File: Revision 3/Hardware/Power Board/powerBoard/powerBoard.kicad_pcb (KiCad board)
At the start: 2 copper layers, 92 x 91.5 mm, 31 parts, among them J1 1366005, J2 1366005, J3 Conn_01x03, J7 Conn_01x02, SW1 SW_SPST, U2 MOC3083S-TA1

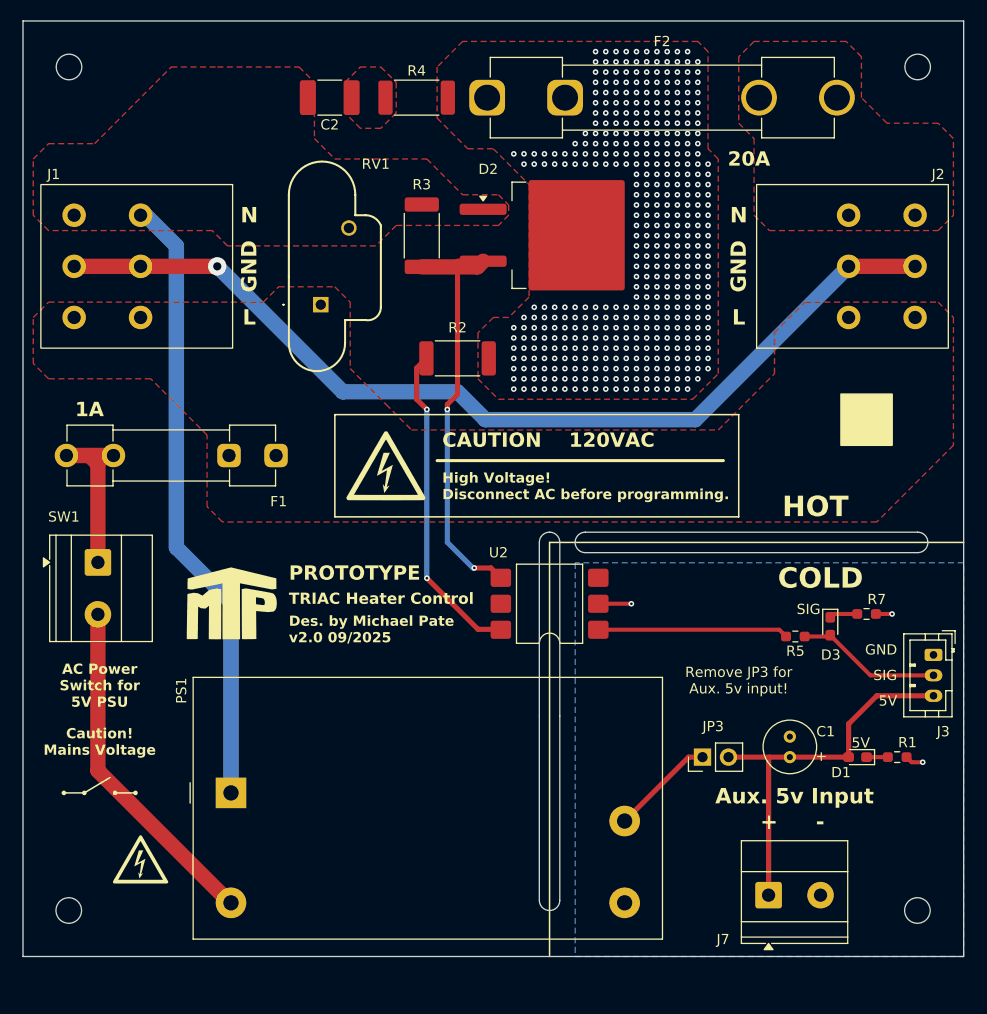
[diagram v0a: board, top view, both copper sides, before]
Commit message: Fix 3D Models, readjust traces on power board
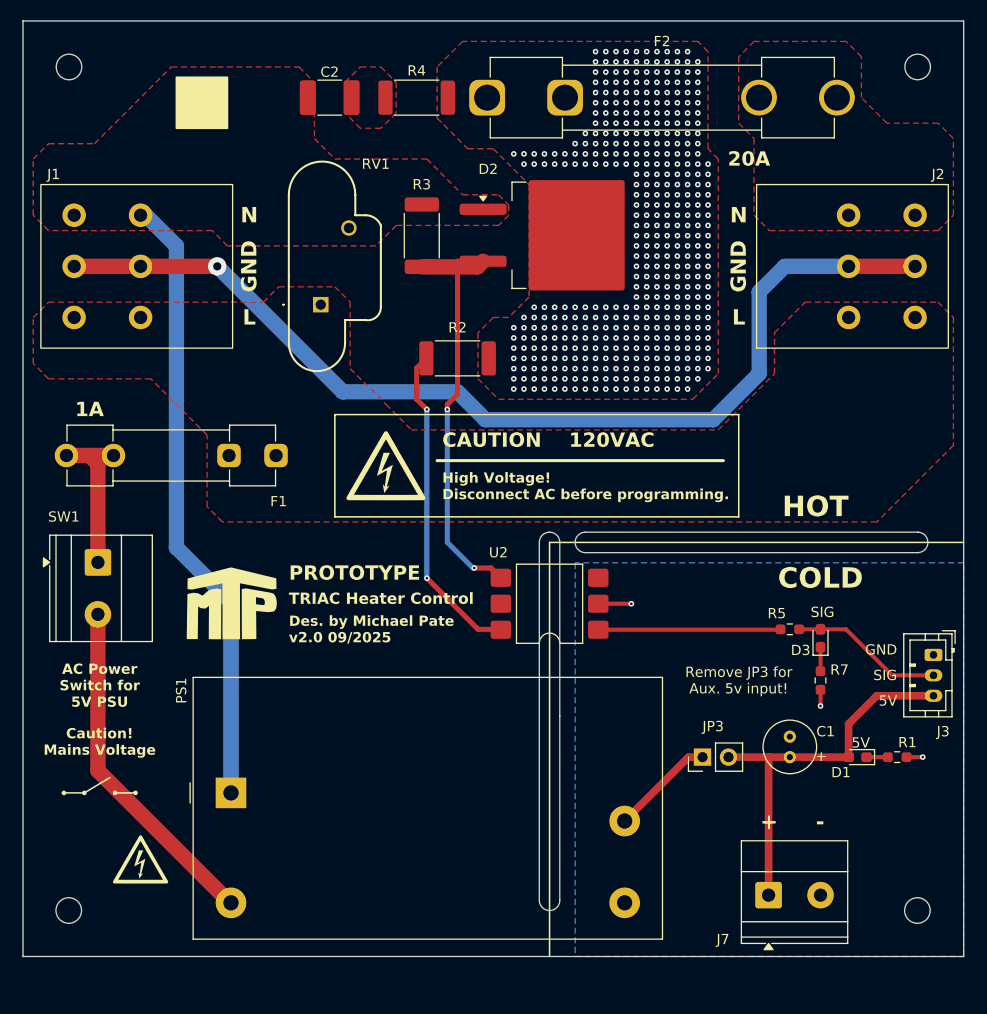
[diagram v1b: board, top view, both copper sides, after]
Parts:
- moved R7 7.91 mm to (191.5, 94.5), turned to -90 degrees
- moved D3 1.51 mm to (191.5, 90.4), turned to 90 degrees
- moved R5 0.89 mm to (188.5, 89.5)
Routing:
- net GNDPWR: track 94.7 -> 99.4 mm
- net /Project Architecture/Heater Control/D_R5_OPTO: track 18.6 -> 17.7 mm
- net /Project Architecture/Heater Control/D3_K: track 2.77 -> 2.21 mm
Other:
- board text removed: "Aux. 5v Input"

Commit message: work on power board layout
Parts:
- removed the G*** at (147.5, 106.5)
- added REF**: MTP Logo 5mm Low Detail, Watermarks:MTP Logo 5mm Low Detail, F.Cu at (200.8, 114.2)
- moved G*** 31.5 mm to (157.8, 97.2)
- moved G*** 4.74 mm to (150.5, 78.0)
- moved F2 3.64 mm to (159.9, 41.0)
- moved C1 3.50 mm to (188.5, 105.5)
- moved C2 3.50 mm to (143.5, 41.0)
- moved D1 3.50 mm to (195.1, 105.5)
- moved D2 3.50 mm to (166.2, 54.5)
- moved D3 3.50 mm to (191.5, 93.9)
- moved F1 3.50 mm to (138.2, 76.0)
- moved G*** 3.50 mm to (125.0, 115.5)
- moved H1 3.50 mm to (118.0, 38.0)
- moved H2 3.50 mm to (201.0, 38.0)
- moved H3 3.50 mm to (118.0, 120.5)
- moved H4 3.50 mm to (201.0, 120.5)
- moved J1 3.50 mm to (131.8, 57.5)
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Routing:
- net GNDPWR: track 99.4 -> 102.0 mm
- net /Project Architecture/Heater Control/L1_F2_OPTO: track 31.6 -> 30.8 mm
- net /Project Architecture/Heater Control/LN_OPTO: track 43.3 -> 43.9 mm
- net LN: vias 0 -> 66
- net /Project Architecture/Heater Control/L1_F2: vias 428 -> 504
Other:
- outline, holes or cut-outs redrawn

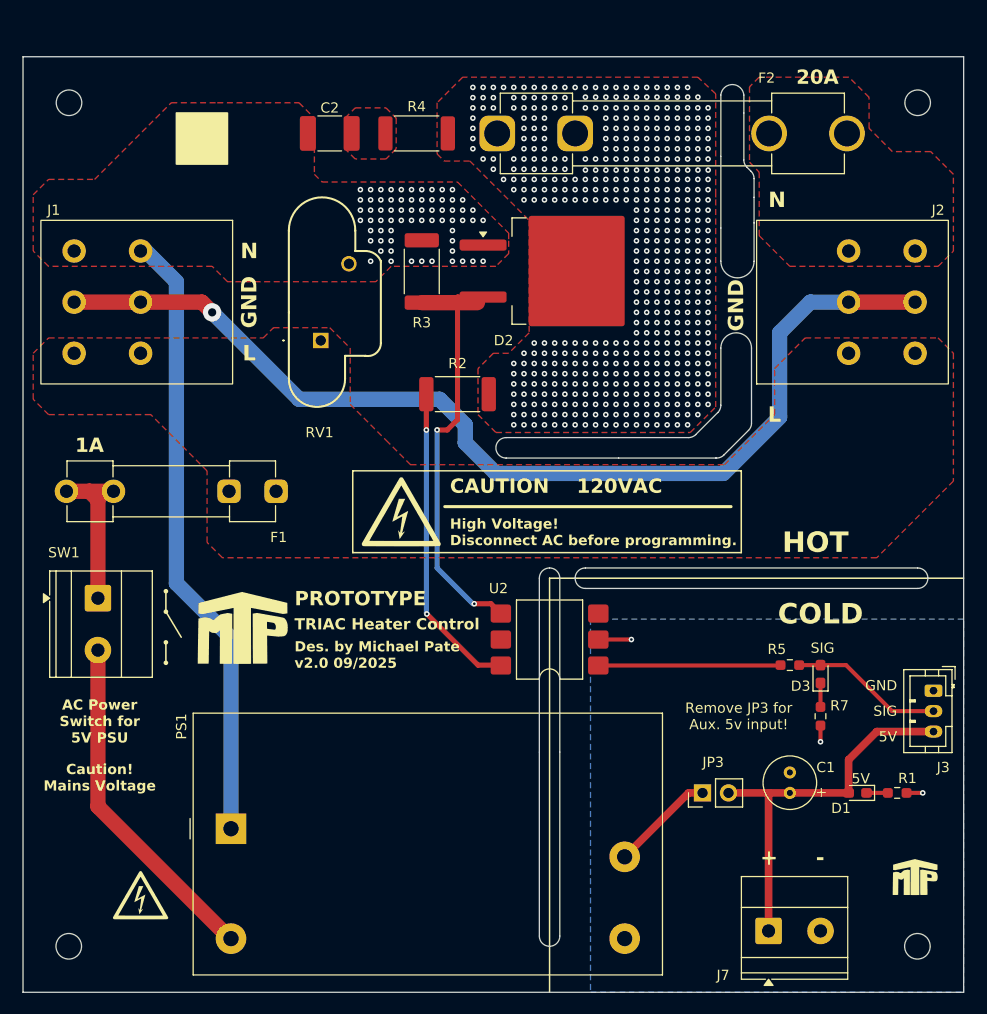
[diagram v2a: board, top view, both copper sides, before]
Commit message: generate gerbers for power board fab
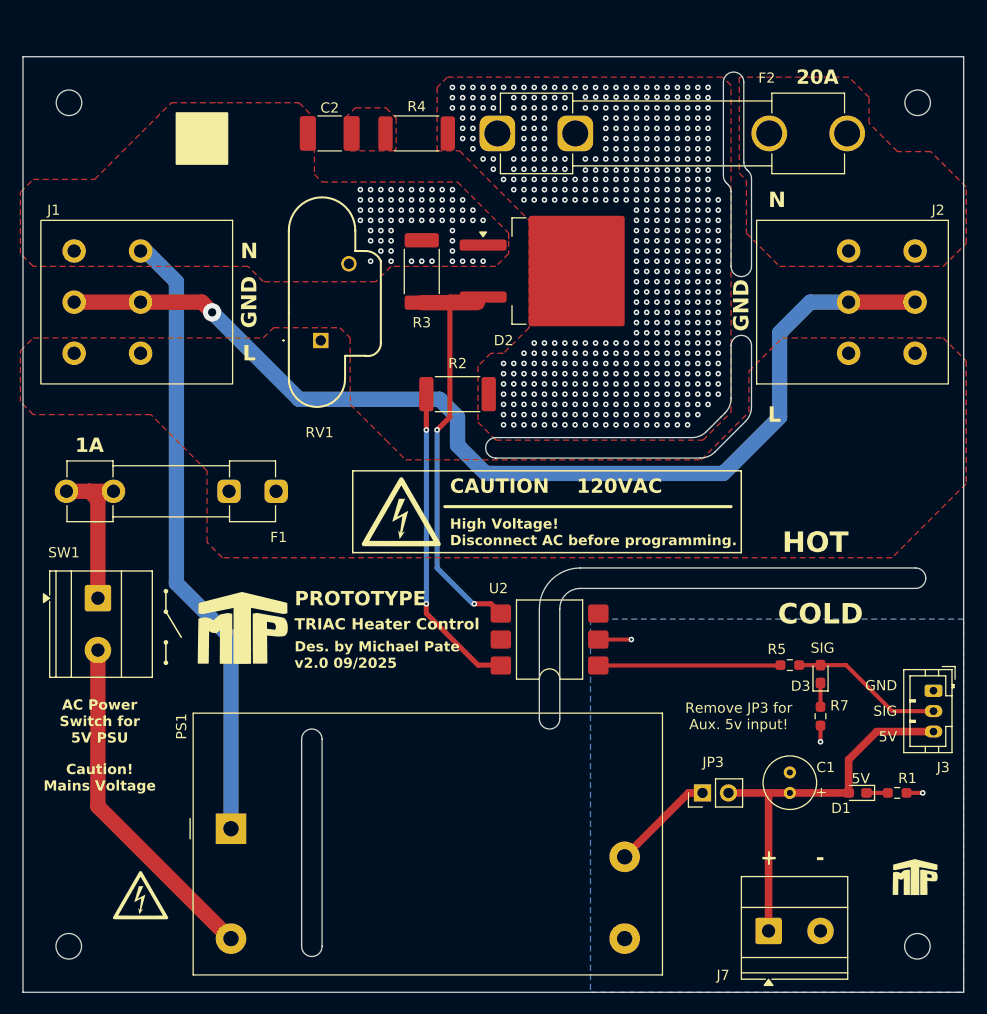
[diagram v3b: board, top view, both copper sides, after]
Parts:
- moved G*** 28.7 mm to (179.0, 78.0)
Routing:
- net GNDPWR: track 102.0 -> 102.6 mm
- net /Project Architecture/Heater Control/L1_F2: vias 504 -> 543
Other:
- outline, holes or cut-outs redrawn
